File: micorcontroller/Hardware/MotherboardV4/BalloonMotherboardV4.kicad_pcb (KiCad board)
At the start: 4 copper layers, 85.9 x 82 mm, 242 parts, among them J1 J1B1211CCD, Y0 ABM8G-12.000MHZ-4Y-T3, Y1 ECS-250-6-33B2-CTP-TR

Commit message: propper Serial Comand System added
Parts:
- added BuckJmp0: Conn_01x03, Connector_PinHeader_2.54mm:PinHeader_1x03_P2.54mm_Vertical, B.Cu at (72.4, 113.5)
- added R87: 10k, Resistor_SMD:R_0603_1608Metric_Pad0.98x0.95mm_HandSolder, F.Cu at (91.9, 41.9)
- added RT0: NTCGS163JF103FT8, SamacSys_Parts:THRMC1608X90N, F.Cu at (90.2, 41.9)
- C11: value 12p -> DNP; footprint Capacitor_SMD:C_0805_2012Metric_Pad1.18x1.45mm_HandSolder -> Capacitor_SMD:C_0402_1005Metric_Pad0.74x0.62mm_HandSolder
- C15: value 10u -> DNP
- C18: value 22u -> DNP
- C38, C39: value Noplace -> DNP
- D0: moved to F.Cu
- R35: value 270 -> 150
- moved D0 50.8 mm to (64.5, 90.4), turned to 0 degrees
- moved R2 44.0 mm to (65.5, 82.3), turned to 180 degrees
- moved JB_or_U0 41.9 mm to (69.6, 84.3), turned to -90 degrees
- moved 5sys0 28.2 mm to (45.7, 56.4), turned to 0 degrees
- moved R6 27.6 mm to (49.5, 56.4)
- moved C72 19.2 mm to (73.7, 100.3)
- moved TP1 10.2 mm to (72.4, 76.2)
- moved TP0 7.62 mm to (70.1, 76.2)
- moved TP2 5.64 mm to (74.7, 76.2)
- moved C69 4.35 mm to (70.6, 87.6)
- moved C73 1.02 mm to (74.7, 86.1), turned to 90 degrees
- moved C11 0.72 mm to (77.7, 104.1)
- turned C10 to -90 degrees
- renumbered MUX to MUX0
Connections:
- net Net-(BUCK0-BST) renamed /Power/BST
- net Net-(BUCK0-FB) renamed /Power/FB
- net Net-(BUCK0-RT) renamed /Power/RT
- net Net-(BUCK0-SS) renamed /Power/SS
- BUCK0 pad 5: Net-(BUCK0-SW) -> /Power/SW
- C10 pad 1: Net-(C10-Pad1) -> /Power/SW
- C10 pad 2: Net-(BUCK0-SW) -> Net-(C10-Pad2)
- C12 pad 2: +28V -> /3V3_rest
- L0 pad 1: Net-(BUCK0-SW) -> /Power/SW
- MUX0 pad 11: unconnected-(MUX0-S6-Pad11) -> Net-(MUX0-S6)
- MUX0 pad 12: unconnected-(MUX0-S5-Pad12) -> Net-(MUX0-S5)
- OP0 pad 8: +28V -> /3V3_rest
- R14 pad 2: Net-(C10-Pad1) -> Net-(C10-Pad2)
- Vref1 pad 3: (no net) -> unconnected-(Vref1-NC-Pad3)
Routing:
- net /Power/VBuck: track 90.0 -> 37.0 mm
- net /Power/V_usb: track 20.2 -> 64.3 mm, vias 0 -> 1
- net /Power/VSys: track 127.3 -> 88.3 mm, vias 0 -> 1
- net GND: track 183.7 -> 170.0 mm, vias 254 -> 261
- net /Prozessor/SWD: track 5.42 -> 16.4 mm
- net +28V: track 106.1 -> 95.7 mm, vias 22 -> 21
- net /3V3_rest: track 196.4 -> 204.2 mm
- net /Prozessor/SWCLK: track 7.98 -> 15.6 mm
- net /Power/3V3_uC: track 35.4 -> 41.7 mm
- net /Power/in-1: track 0.00 -> 4.86 mm
- net /Prozessor/scloxy: track 73.0 -> 68.6 mm
- net /Power/in+1: track 0.33 -> 4.75 mm
- net Net-(MUX0-S6): track 0.00 -> 3.79 mm
- net /Power/ADC_curr: track 47.3 -> 51.1 mm
- net Net-(MUX0-S5): track 0.00 -> 3.05 mm
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- added copper zone on In2.Cu, net +28V
- added copper zone on F.Cu, net /Power/SW
- removed copper zone on F.Cu, net /Power/ADC_curr
- removed copper zone on F.Cu, net /Power/in+1
- removed copper zone on F.Cu, net /Power/in-1
- removed copper zone on F.Cu, net Net-(BUCK0-SW)
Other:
- board text added: "3v3_Rest"
- board text added: "3v3_SD/LAN"
- board text added: "3v3_uC"
- board text added: "5V"
- board text added: "ba|heat"
- board text added: "bu|sy|usb"
- board text added: "gn|ba|bu"
- board text added: "ntc"
- board text removed: "b"
- board text removed: "h"
- board text removed: "u"

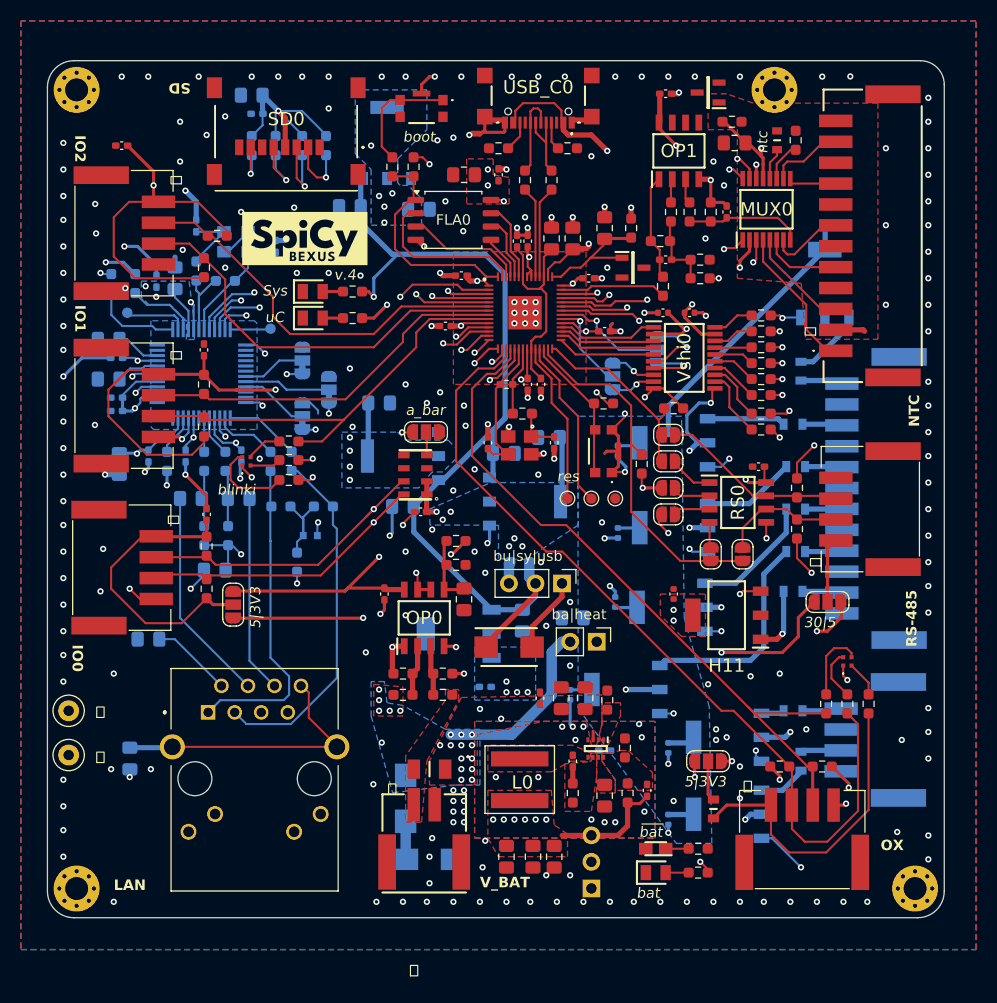
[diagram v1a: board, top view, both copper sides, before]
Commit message: added a serial command field for easy debugging
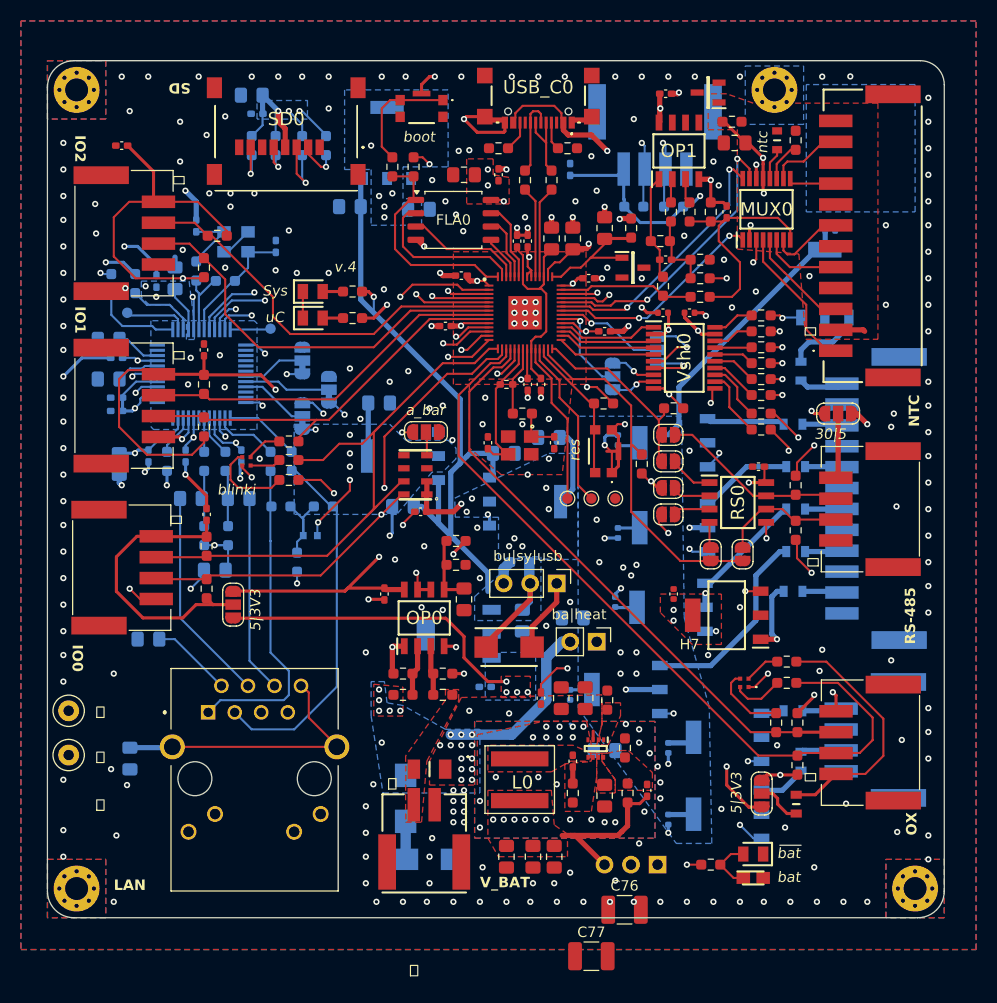
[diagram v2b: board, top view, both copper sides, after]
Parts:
- removed R1: 12k, Resistor_SMD:R_0603_1608Metric_Pad0.98x0.95mm_HandSolder
- added C75: 0.1u, Capacitor_SMD:C_0402_1005Metric_Pad0.74x0.62mm_HandSolder, B.Cu at (70.4, 44.7)
- added C76: DNP, Capacitor_SMD:C_1210_3225Metric_Pad1.33x2.70mm_HandSolder, F.Cu at (75.6, 115.6)
- added C77: DNP, Capacitor_SMD:C_1210_3225Metric_Pad1.33x2.70mm_HandSolder, F.Cu at (72.4, 120.0)
- added GPIO3: 502352-0400, SamacSys_Parts:5023520400, B.Cu at (78.5, 41.4)
- added L1: InstaLogo, SamacSys_Parts:insta, F.Cu at (98.0, 42.7)
- added R88: 0 DNP, Resistor_SMD:R_0603_1608Metric_Pad0.98x0.95mm_HandSolder, F.Cu at (82.8, 56.9)
- added R89: 4.7k, Resistor_SMD:R_0603_1608Metric_Pad0.98x0.95mm_HandSolder, B.Cu at (76.5, 48.3)
- added R90: 4.7k, Resistor_SMD:R_0603_1608Metric_Pad0.98x0.95mm_HandSolder, B.Cu at (80.3, 48.3)
- C14: value 10u -> 10u/30V
- C17: value 0.1u -> 0.1u/30V
- C69: value 1u/40V -> 1u/30V DNP
- C72: value 0.1u/40V -> 0.1u/30V DNP; footprint Capacitor_SMD:C_0402_1005Metric_Pad0.74x0.62mm_HandSolder -> Capacitor_SMD:C_0805_2012Metric_Pad1.18x1.45mm_HandSolder
- R26, R37: value 5k -> 5.1k
- R39: value 72,5k -> 6,5k
- R85, R86: value 100 -> 4,7k
- moved JP9 18.1 mm to (96.0, 68.1)
- moved Ox0 11.3 mm to (99.1, 99.6), turned to 90 degrees
- moved LED1 10.1 mm to (87.0, 93.8), turned to -90 degrees
- moved !bat0 9.74 mm to (87.9, 112.5), turned to 0 degrees
- moved bat0 9.50 mm to (87.9, 110.2), turned to 180 degrees
- moved R41 8.81 mm to (91.1, 91.8), turned to 0 degrees
- moved F0 7.94 mm to (92.0, 105.5), turned to -90 degrees
- moved BuckJmp0 6.73 mm to (78.7, 111.3), turned to 90 degrees
- moved R40 6.14 mm to (91.1, 93.8), turned to 180 degrees
- moved JPVOX1 5.99 mm to (88.7, 104.4), turned to 90 degrees
- moved R42 5.11 mm to (90.1, 97.7)
- moved R46 4.82 mm to (92.1, 97.7), turned to 90 degrees
- moved R50 4.19 mm to (91.9, 74.9), turned to -90 degrees
- moved R49 4.07 mm to (91.9, 79.2), turned to 90 degrees
- moved R0 1.94 mm to (83.8, 111.3), turned to 180 degrees
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- renumbered H4 to H0, H0 to H0_M0, H5 to H1, H1 to H1_M0, H6 to H2, H2 to H2_M0, H7 to H3, H3 to H3_M0, H8 to H4, H9 to H5, H10 to H6, H11 to H7
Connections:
- net Net-(JH0-C) renamed /EthernetaSD/E2
- net Net-(JH1-C) renamed /EthernetaSD/E1
- net Net-(JH2-C) renamed /EthernetaSD/E0
- H0_M0 pad 1: (no net) -> GND
- H1_M0 pad 1: (no net) -> GND
- H2_M0 pad 1: (no net) -> GND
- H3_M0 pad 1: (no net) -> GND
- R39 pad 1: /5V -> /Sensors/ntc+
- R49 pad 2: /Sensors/B -> /Sensors/A
- R50 pad 2: /Sensors/A -> /Sensors/B
- RS-0 pad 1: GND -> Net-(JP9-C)
- RS-0 pad 4: Net-(JP9-C) -> GND
- bat0 pad 2: Net-(bat0-A) -> Net-(!bat0-K)
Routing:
- net /5V: track 65.2 -> 130.5 mm, vias 12 -> 7
- net /EthernetaSD/mosi_sd: track 29.5 -> 80.1 mm, vias 2 -> 3
- net /EthernetaSD/sck_sd: track 30.6 -> 68.5 mm, vias 2 -> 3
- net /3V3_rest: track 204.2 -> 224.5 mm, vias 21 -> 25
- net +28V: track 95.7 -> 110.9 mm, vias 21 -> 22
- net GND: track 170.0 -> 158.2 mm, vias 261 -> 305
- net /Sensors/ntc -: track 11.2 -> 22.4 mm
- net /Prozessor/scloxy: track 68.6 -> 58.1 mm
- net /Sensors/ntc+: track 3.13 -> 12.8 mm, vias 0 -> 2
- net /Power/VSys: track 88.3 -> 79.0 mm
- net Net-(H1-IN): track 52.2 -> 43.1 mm, vias 4 -> 2
- net /Prozessor/sdaoxy: track 81.5 -> 75.2 mm
- net /Sensors/Vox: track 29.8 -> 24.0 mm
- net /Power/VBuck: track 37.0 -> 42.1 mm
- net /3V3lan: track 144.1 -> 139.7 mm, vias 18 -> 20
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- added copper zone on B.Cu, net (none)
- added copper zone on In2.Cu, net /3V3lan
- added copper zone on F.Cu, net /5V
- added copper zone on In2.Cu, net /Power/3V3_uC
- added copper zone on In2.Cu, net /Power/VBuck
- added copper zone on B.Cu, net /Power/VSys
- removed copper zone on In1.Cu, net /3V3lan
- removed copper zone on In1.Cu, net /5V
- removed copper zone on In1.Cu, net /Power/3V3_uC
- removed copper zone on In1.Cu, net /Power/VBuck
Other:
- board text added: "3v3 Rest"
- board text added: "3v3 SD"
- board text added: "3v3 uC"
- board text added: "Fynn Gewiese 0176-29960317 spicy-bexus@bio.lmu.de"
- board text added: "IO3"
- board text removed: "3v3_Rest"
- board text removed: "3v3_SD/LAN"
- board text removed: "3v3_uC"

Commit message: Switch to header BASED C file system {headache incomming}
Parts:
- removed the C18 at (68.8, 110.5)
- removed the C38 at (85.3, 48.8)
- removed the R37 at (83.8, 48.8)
- removed R88: 0 DNP, Resistor_SMD:R_0603_1608Metric_Pad0.98x0.95mm_HandSolder
- added C41: DNP, Capacitor_SMD:C_0402_1005Metric_Pad0.74x0.62mm_HandSolder, F.Cu at (89.7, 50.3)
- added G***: LOGO, LOGO, F.Cu at (100.2, 76.9)
- added G***: LOGO, LOGO, F.Cu at (59.2, 49.3)
- added G***: LOGO, LOGO, F.Cu at (35.3, 99.3)
- added G***: LOGO, LOGO, F.Cu at (64.5, 37.1)
- added G***: LOGO, LOGO, B.Cu at (94.8, 55.7)
- added G***: LOGO, LOGO, B.Cu at (52.8, 42.2)
- added G***: LOGO, LOGO, B.Cu at (101.9, 59.7)
- added G***: LOGO, LOGO, B.Cu at (35.3, 64.3)
- added G***: LOGO, LOGO, B.Cu at (78.5, 40.8)
- added G***: LOGO, LOGO, B.Cu at (59.7, 88.9)
- added G***: LOGO, LOGO, B.Cu at (80.3, 79.0)
- added G***: LOGO, LOGO, F.Cu at (27.2, 50.8)
- added G***: LOGO, LOGO, B.Cu at (85.3, 99.1)
- added G***: LOGO, LOGO, B.Cu at (102.1, 91.4)
- added G***: LOGO, LOGO, B.Cu at (54.4, 72.1)
- added G***: LOGO, LOGO, B.Cu at (66.0, 76.5)
- added G***: LOGO, LOGO, B.Cu at (80.0, 86.6)
- added G***: LOGO, LOGO, B.Cu at (75.7, 94.5)
- added G***: LOGO, LOGO, B.Cu at (80.3, 70.9)
- added G***: LOGO, LOGO, B.Cu at (85.3, 106.7)
- added G***: LOGO, LOGO, F.Cu at (101.1, 50.8)
- added G***: LOGO, LOGO, F.Cu at (26.9, 67.6)
- added G***: LOGO, LOGO, F.Cu at (100.8, 99.3)
- added G***: LOGO, LOGO, F.Cu at (56.7, 99.7)
- added G***: LOGO, LOGO, F.Cu at (85.3, 87.4)
- added G***: LOGO, LOGO, F.Cu at (27.2, 82.5)
- added R39: 5.1k, Resistor_SMD:R_0603_1608Metric_Pad0.98x0.95mm_HandSolder, F.Cu at (92.2, 61.0)
- added R40: 5.1k, Resistor_SMD:R_0603_1608Metric_Pad0.98x0.95mm_HandSolder, F.Cu at (92.2, 57.1)
- added R42: 5.1k, Resistor_SMD:R_0603_1608Metric_Pad0.98x0.95mm_HandSolder, F.Cu at (92.3, 53.1)
- added R44: 5.1k, Resistor_SMD:R_0603_1608Metric_Pad0.98x0.95mm_HandSolder, F.Cu at (92.2, 49.0)
- added R50: 5.1k, Resistor_SMD:R_0603_1608Metric_Pad0.98x0.95mm_HandSolder, F.Cu at (92.2, 45.2)
- added R51: 5.1k, Resistor_SMD:R_0603_1608Metric_Pad0.98x0.95mm_HandSolder, F.Cu at (91.2, 42.2)
- added R52: 5.1k, Resistor_SMD:R_0603_1608Metric_Pad0.98x0.95mm_HandSolder, F.Cu at (87.6, 42.7)
- added R54: 5.1k, Resistor_SMD:R_0603_1608Metric_Pad0.98x0.95mm_HandSolder, F.Cu at (90.4, 48.0)
- C10: renamed from C76; footprint Capacitor_SMD:C_1210_3225Metric_Pad1.33x2.70mm_HandSolder -> Capacitor_SMD:C_0805_2012Metric_Pad1.18x1.45mm_HandSolder
- C20: renamed from C77; footprint Capacitor_SMD:C_1210_3225Metric_Pad1.33x2.70mm_HandSolder -> Capacitor_SMD:C_0805_2012Metric_Pad1.18x1.45mm_HandSolder
- moved C10 20.7 mm to (71.4, 95.2), turned to -90 degrees
- moved C20 14.1 mm to (63.2, 109.2), turned to 90 degrees
- moved C75 11.8 mm to (83.6, 94.0), turned to 0 degrees
- moved C8 8.17 mm to (64.0, 97.8), turned to 90 degrees
- moved C18 8.13 mm to (61.7, 104.1), turned to -90 degrees
- moved C12 7.90 mm to (61.5, 100.3), turned to 180 degrees
- moved C15 7.40 mm to (74.8, 107.4), turned to 90 degrees
- moved R60 6.82 mm to (88.9, 48.0)
- moved C17 6.36 mm to (64.0, 104.1), turned to -90 degrees
- moved R13 4.20 mm to (74.8, 104.3), turned to -90 degrees
- moved C11 4.15 mm to (73.7, 95.2)
- moved L1 4.09 mm to (69.6, 103.7), turned to -90 degrees
- moved MUX0 4.07 mm to (85.1, 48.3)
- moved C62 3.81 mm to (43.7, 37.6), turned to 180 degrees
- moved C22 3.59 mm to (31.0, 42.9), turned to 0 degrees
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- renumbered C15 to C11, C17 to C12, C9 to C13, C12 to C14, C10 to C15, C11 to C16, C13 to C17, C16 to C18, C22 to C21, C19 to C22, C75 to C23, C21 to C24, C20 to C25, C23 to C26, C24 to C27, C25 to C28, C26 to C29, C27 to C30, C28 to C31, C29 to C32, C30 to C33, C31 to C34, C32 to C35, C33 to C36, C34 to C37, C35 to C38, C36 to C39, C37 to C40, C39 to C42, C41 to C43, C40 to C44, C42 to C45, C43 to C46, C44 to C47, C45 to C48, C46 to C49, C47 to C50, C48 to C51, C49 to C52, C50 to C53, C51 to C54, C52 to C55, C53 to C56, C54 to C57, C55 to C58, C56 to C59, C57 to C60, C58 to C61, C59 to C62, C60 to C63, C61 to C64, C62 to C65, C63 to C66, C64 to C67, C65 to C68, C66 to C69, C67 to C70, C68 to C71, C69 to C72, C70 to C73, C71 to C74, C72 to C75, C73 to C76, C74 to C77, C14 to C8, C8 to C9, GPIO3 to GPIO1, GPIO1 to GPIO3, JP5 to JP3, JP6 to JP4, JP7 to JP5, JP8 to JP6, JP3 to JP7, JP4 to JP8, L1 to L0, L0 to L1, R2 to R1, R12 to R10, R13 to R12, R14 to R13, R15 to R14, R16 to R15, R17 to R16, R89 to R17, R19 to R18, R18 to R19, R90 to R21, R21 to R23, R23 to R24, R24 to R25, R25 to R26, R26 to R27, R27 to R28, R28 to R29, R29 to R30, R30 to R31, R31 to R32, R32 to R33, R33 to R34, R34 to R35, R35 to R36, R36 to R37, R5 to R4, R38 to R41, R39 to R43, R40 to R45, R41 to R46, R42 to R47, R43 to R48, R44 to R49, R6 to R5, R45 to R53, R46 to R55, R47 to R56, R48 to R57, R86 to R58, R85 to R59, R7 to R6, R87 to R60, R49 to R61, R50 to R62, R51 to R63, R52 to R64, R53 to R65, R54 to R66, R55 to R67, R56 to R68, R57 to R69, R8 to R7, R58 to R70, R59 to R71, R60 to R72, R61 to R73, R62 to R74, R63 to R75, R64 to R76, R65 to R77, R66 to R78, R67 to R79, R9 to R8, R68 to R80, R72 to R84, R73 to R85, R74 to R86, R10 to R9, R78 to R90, R79 to R91, R80 to R92, R83 to R95, R84 to R96
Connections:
- net Net-(MUX0-S5) renamed /Sensors/NTC6
- net Net-(MUX0-S6) renamed /Sensors/NTC7
- BuckJmp0 pad 3: /Power/VBuck -> /Power/VBUCK
- C16 pad 1: /Power/VBuck -> /Power/VBUCK
- C17 pad 2: /Power/VBuck -> /Power/VBUCK
- C18 pad 2: /Power/VBuck -> /Power/VBUCK
- C20 pad 2: /Power/VBuck -> /Power/VBUCK
- C43 pad 2: /3V3_rest -> /Power/3V3_uC
- C44 pad 1: /3V3_rest -> /Power/3V3_uC
- JB_or_U0 pad 3: /Power/VBuck -> /Power/VBUCK
- JPVOX1 pad 1: /5V -> /Power/VBUCK
- L1 pad 2: /Power/VBuck -> /Power/VBUCK
- MUX0 pad 13: /3V3_rest -> /Power/3V3_uC
- MUX0 pad 2: /3V3_rest -> /Power/3V3_uC
- OP1 pad 8: /3V3_rest -> /Power/3V3_uC
- R1 pad 2: /Power/VBuck -> /Power/VBUCK
- R14 pad 2: /Power/VBuck -> /Power/VBUCK
- R37 pad 1: /3V3_rest -> /Power/3V3_uC
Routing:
- net /Power/VBUCK: track 0.00 -> 64.7 mm, vias 0 -> 6
- net /Power/VBuck: track 42.1 -> 0.00 mm, vias 6 -> 0
- net /Power/3V3_uC: track 41.4 -> 79.1 mm, vias 19 -> 24
- net /3V3_rest: track 224.5 -> 251.4 mm, vias 25 -> 21
- net /Sensors/ntc+: track 12.8 -> 30.0 mm, vias 2 -> 12
- net /5V: track 130.5 -> 116.0 mm, vias 7 -> 6
- net /Sensors/ntc -: track 22.4 -> 9.90 mm
- net /Power/FB: track 0.00 -> 10.6 mm
- net /Power/SW: track 0.00 -> 7.03 mm
- net /Sensors/NTC4: track 3.14 -> 8.78 mm
- net /Prozessor/A2: track 28.2 -> 23.0 mm
- net /Sensors/NTC1: track 10.5 -> 15.7 mm
- net /Sensors/NTC5: track 6.95 -> 11.2 mm
- net /Sensors/NTC2: track 7.26 -> 11.5 mm
- net /Sensors/NTC3: track 7.83 -> 11.5 mm
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- added copper zone on In1.Cu, net /5V
- added copper zone on F.Cu, net /Power/VBUCK
- added copper zone on In2.Cu, net /Power/VBUCK
- added copper zone on In1.Cu, net /Sensors/ntc+
- removed copper zone on In2.Cu, net /5V
- removed copper zone on F.Cu, net /Power/BST
- removed copper zone on F.Cu, net /Power/FB
- removed copper zone on F.Cu, net /Power/SS
- removed copper zone on F.Cu, net /Power/VBuck
- removed copper zone on In2.Cu, net /Power/VBuck
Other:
- board text added: "#great efficiency"
- board text added: "6|3V3"
- board text added: "Big Boy USART"
- board text added: "Fancy Flash. Bigger than usual"
- board text added: "I04"
- board text added: "IO5"
- board text added: "Small step for Humanity"
- board text added: "spicy-bexus@bio.lmu.de"
- board text removed: "Fynn Gewiese 0176-29960317 spicy-bexus@bio.lmu.de"
- board text removed: "a_bar"

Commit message: added uplink
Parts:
- C3: value 0.22uF -> 4.7u
- C7: value 0.1u -> 1u
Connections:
- Vref1 pad 3: unconnected-(Vref1-NC-Pad3) -> (no net)
